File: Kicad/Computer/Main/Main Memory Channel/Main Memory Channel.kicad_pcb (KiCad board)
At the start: 2 copper layers, 18.8 x 53.5 mm, 14 parts, among them IC1 74LVC541APW,118, IC2 74LVC573APW,118, IC3 74LVC138APW-Q100J, IC4 74LVC573APW,118, IC5 AP7365-33WG-7, IC7 74LVC04APW,118, J4 Conn_02x20_Counter_Clockwise

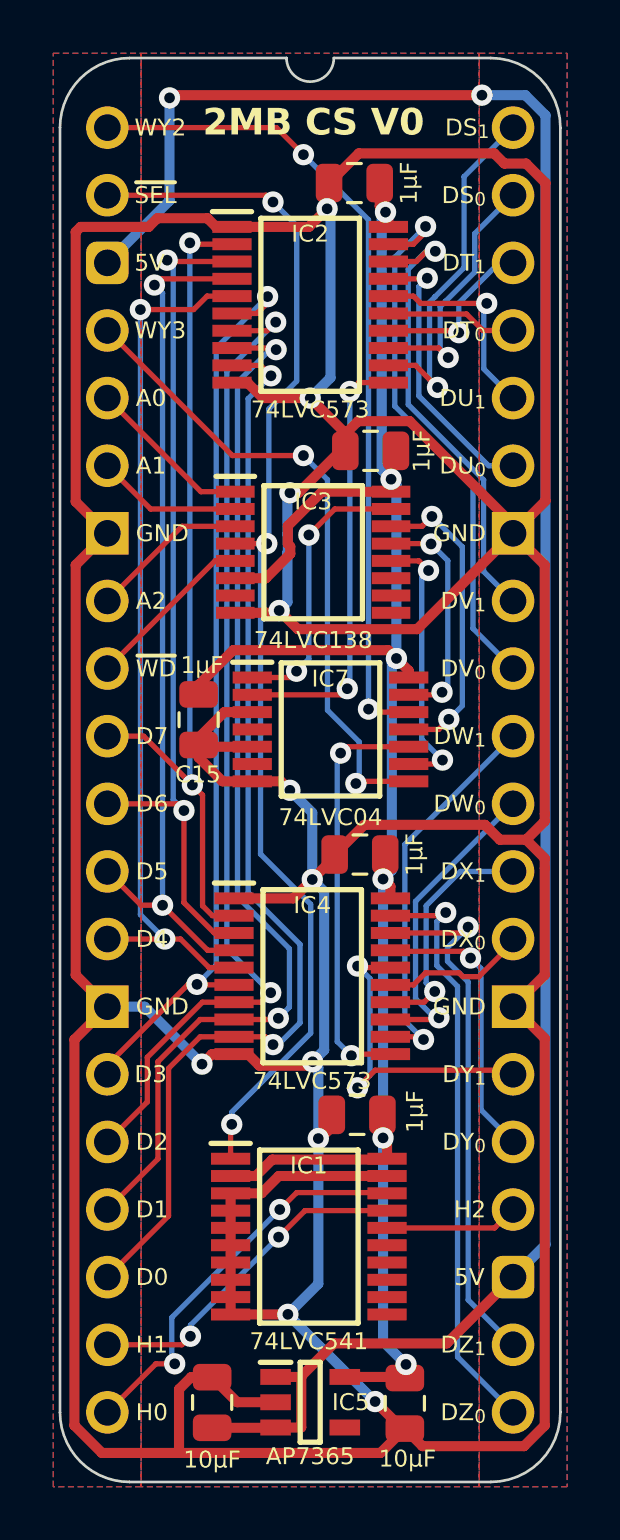
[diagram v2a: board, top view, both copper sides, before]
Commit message: Added a TTL5V UART.
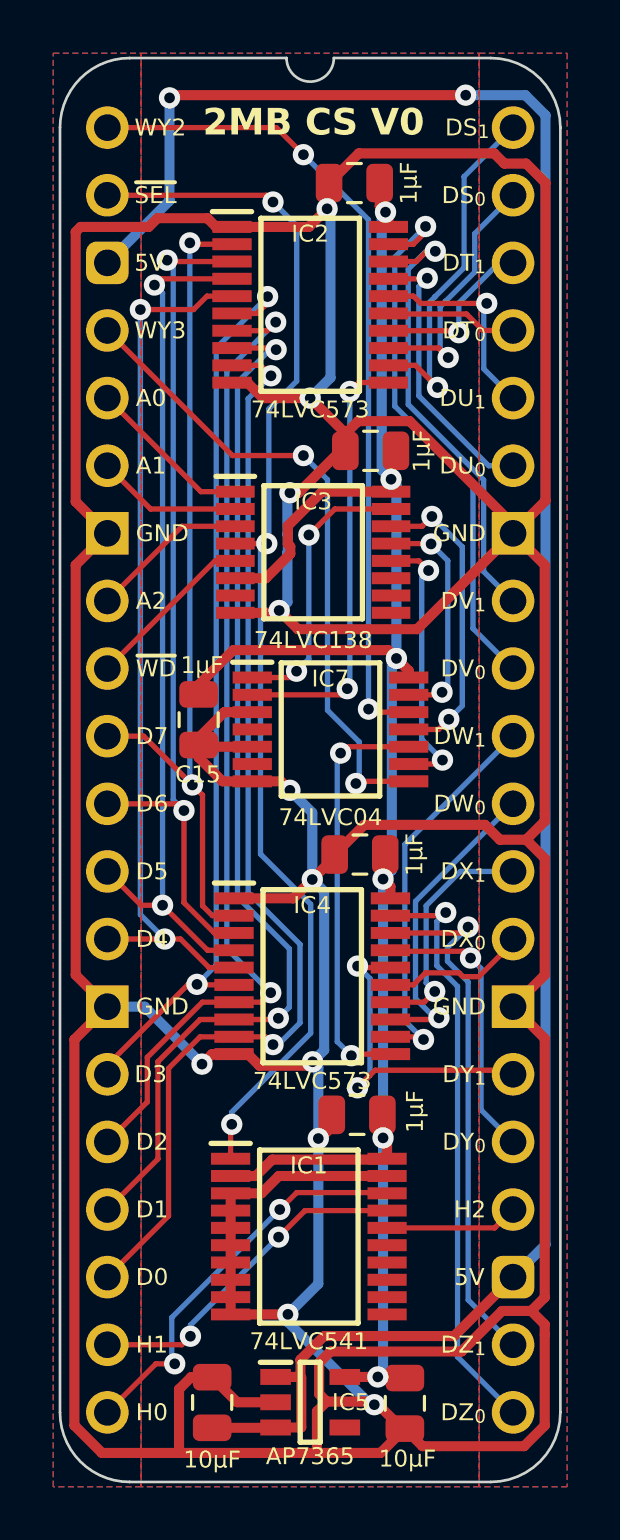
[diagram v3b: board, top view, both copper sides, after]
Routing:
- net GND: track 253.3 -> 268.1 mm
- net /3.3V: track 76.8 -> 77.5 mm

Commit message: Generated Gerbers for the Mainboard Small and Components.
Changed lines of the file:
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@@
 		(fp_arc
 			(start 14.404267 -2.613733)
-			(mid 16.252448 -1.848183)
+			(mid 16.252451 -1.848184)
 			(end 17.017999 -0.000001)
 			(stroke

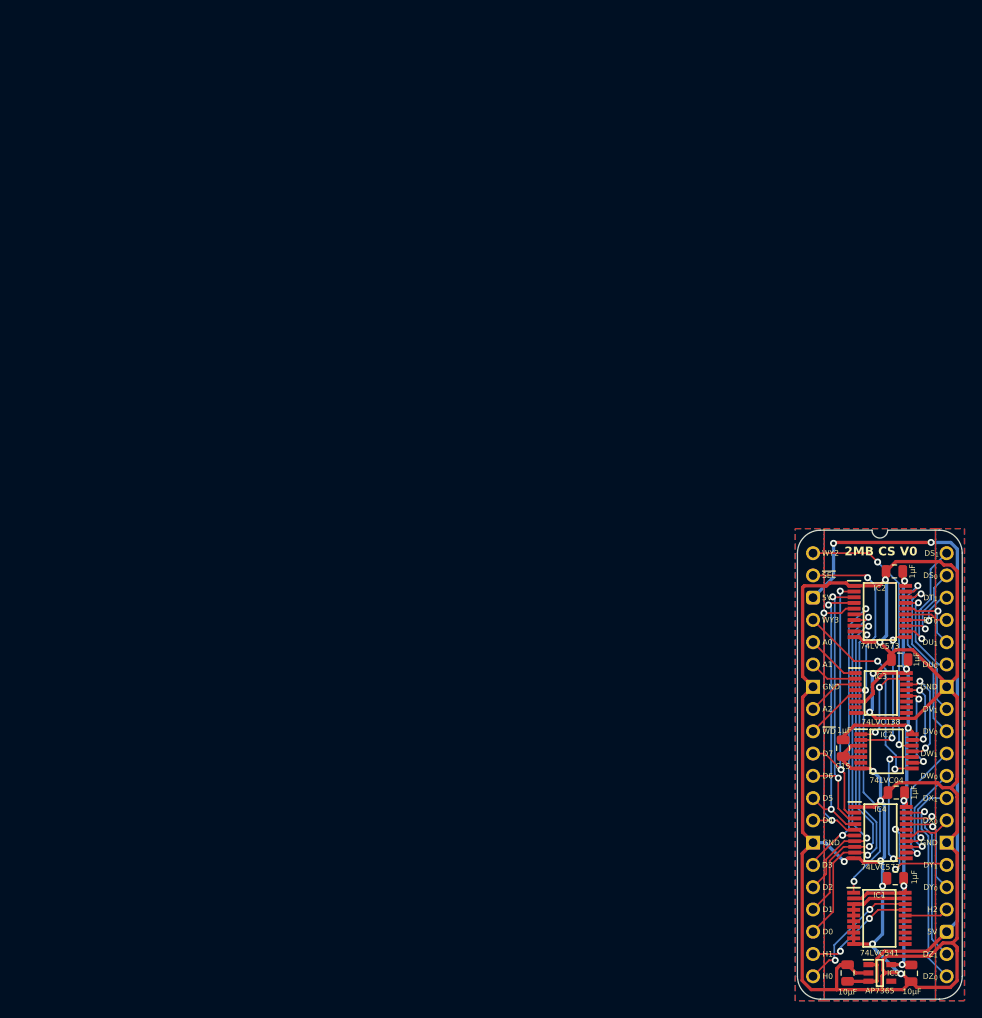
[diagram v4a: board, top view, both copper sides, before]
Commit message: Use VRML instead of STEPs for Main Board models.
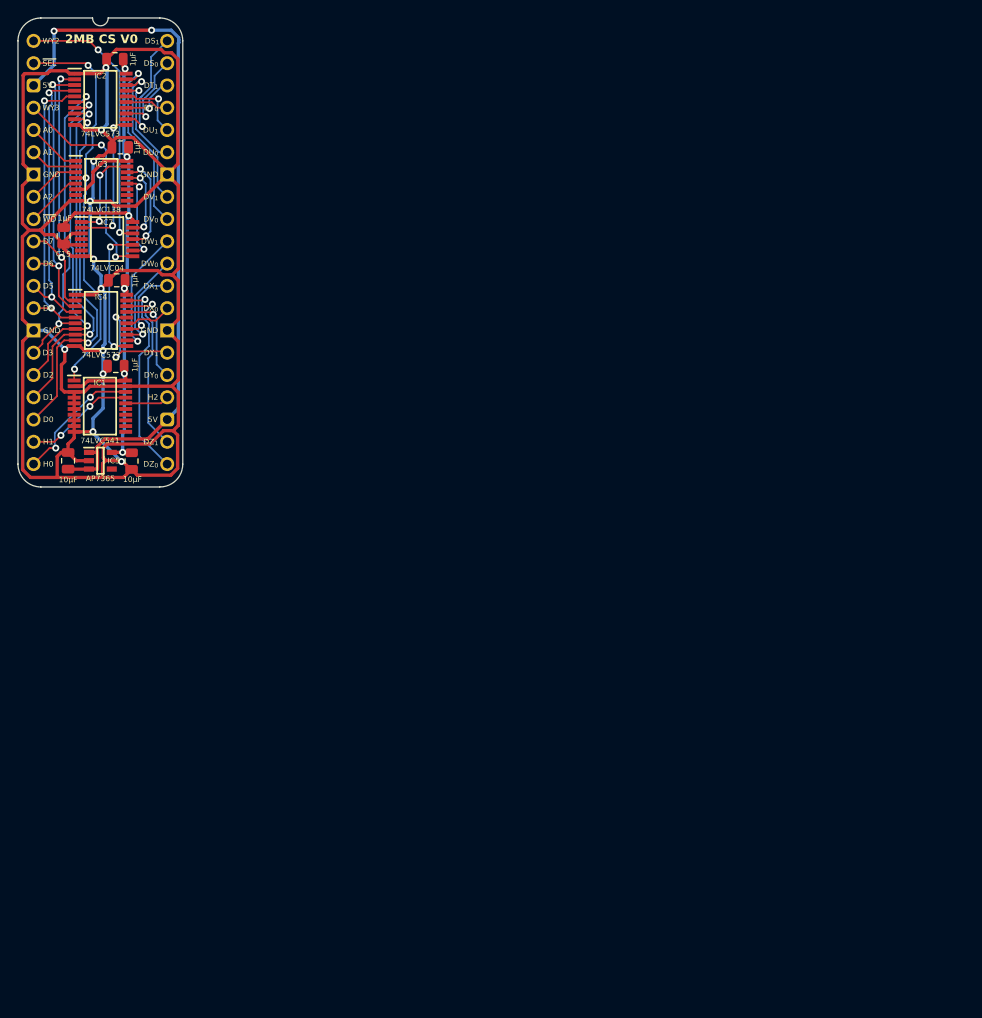
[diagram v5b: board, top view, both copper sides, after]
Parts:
- added J1: Pin_Header_01x20, SamacSys_Parts:PinHeader_1x20_P2.54mm_Vertical, B.Cu at (15.2, 0.00)
- added J2: Pin_Header_01x20, SamacSys_Parts:PinHeader_1x20_P2.54mm_Vertical, B.Cu at (0.00, 0.00)
- moved C5 106.4 mm to (9.40, 37.1)
- moved C8 106.4 mm to (3.94, 47.9)
- moved IC1 106.4 mm to (7.57, 41.7)
- moved IC4 106.4 mm to (7.70, 31.9)
- moved J4 106.4 mm to (0.00, 0.00)
- moved C10 106.4 mm to (9.51, 27.3)
- moved C15 106.4 mm to (3.43, 22.2)
- moved C6 106.4 mm to (9.91, 12.1)
- moved C7 106.4 mm to (9.30, 2.08)
- moved C9 106.4 mm to (11.2, 47.9)
- moved IC2 106.4 mm to (7.62, 6.65)
- moved IC3 106.4 mm to (7.73, 16.0)
- moved IC5 106.4 mm to (7.62, 47.9)
- moved IC7 106.4 mm to (8.38, 22.6)
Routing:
- net GND: track 268.1 -> 300.5 mm
- net D3: track 34.7 -> 35.8 mm
- net Device_{(Z)} 2MB Select_{0}: track 22.2 -> 23.1 mm
- removed copper zone on B.Cu, net GND
- removed copper zone on F.Cu, net GND

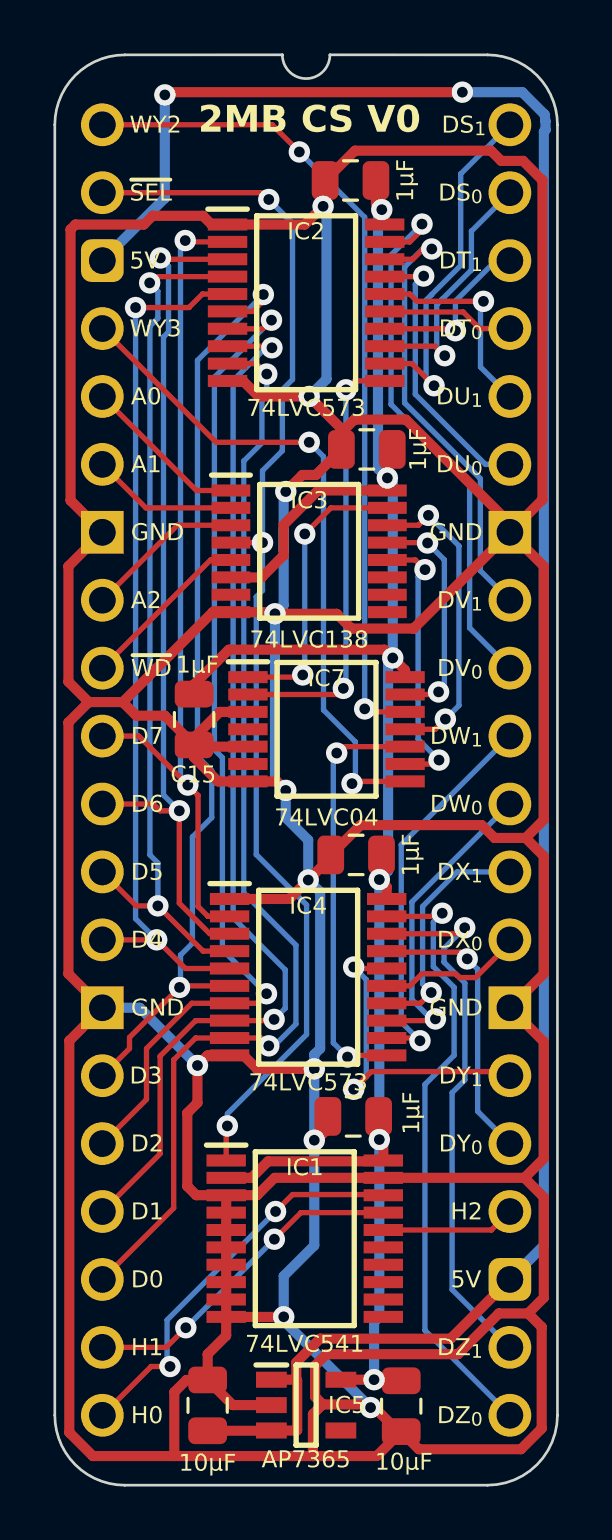
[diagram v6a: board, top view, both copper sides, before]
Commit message: Rounded Main Memory Channel traces.
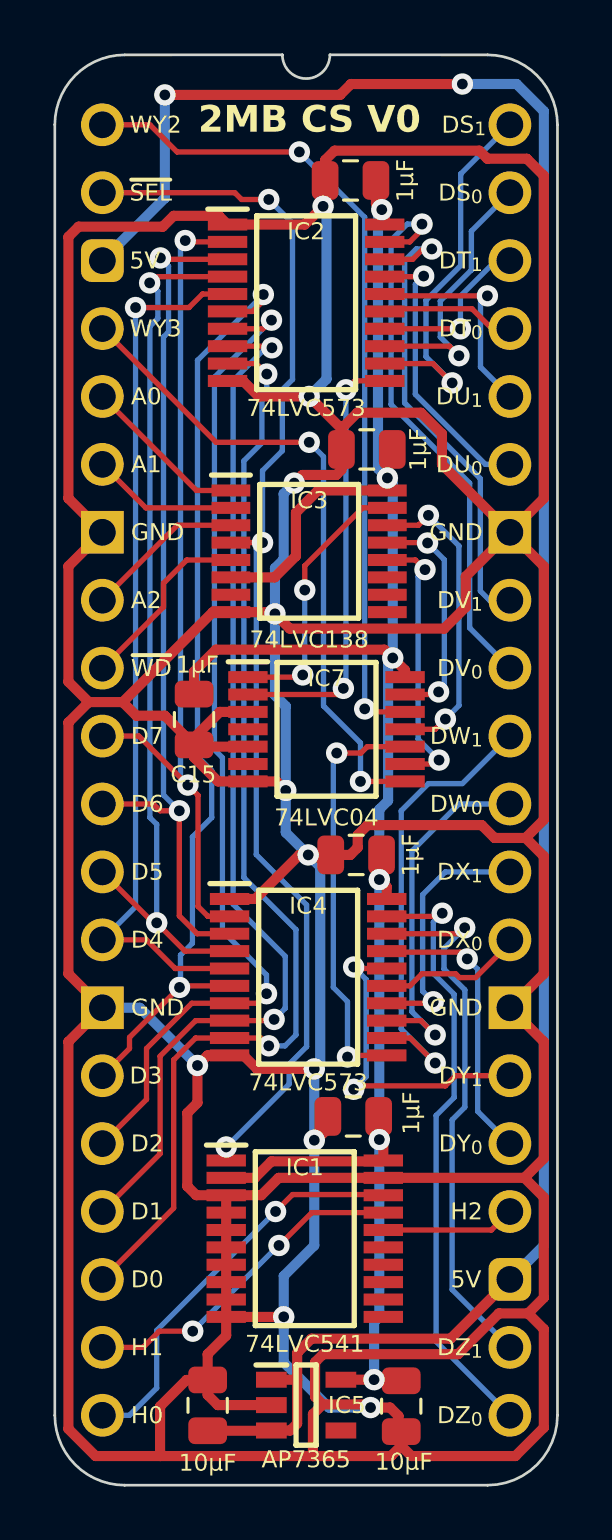
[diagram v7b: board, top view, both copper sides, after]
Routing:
- net GND: track 300.5 -> 305.1 mm
- net Device_{(W)} 2MB Select_{1}: track 14.7 -> 17.4 mm
- net Device_{(W)} 2MB Select_{0}: track 11.9 -> 13.7 mm
- net Device_{(S)} 2MB Select_{1}: track 13.4 -> 14.2 mm
- net Device_{(T)} 2MB Select_{0}: track 4.92 -> 4.16 mm
- net /~{WY_{0}}: track 10.9 -> 10.2 mm
- net Device_{(S)} 2MB Select_{0}: track 9.75 -> 10.4 mm
- net D5: track 32.7 -> 33.3 mm
- net Device_{(V)} 2MB Select_{1}: track 17.3 -> 17.9 mm
- net Device_{(X)} 2MB Select_{1}: track 8.98 -> 9.55 mm
- net /3.3V: track 77.4 -> 78.0 mm
- net ~{WD}: track 6.48 -> 7.00 mm
- net D4: track 32.8 -> 33.0 mm, vias 2 -> 1
- net H0: track 15.1 -> 15.2 mm, vias 2 -> 1
